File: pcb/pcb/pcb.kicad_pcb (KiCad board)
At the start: 2 copper layers, 58.4 x 44.4 mm, 20 parts, among them J1 UART, J2 Barrel_Jack, J3 Stepper, SW1 RESET, SW2 FLASH, U1 ESP32-WROOM-32, U2 TSR_1-2433

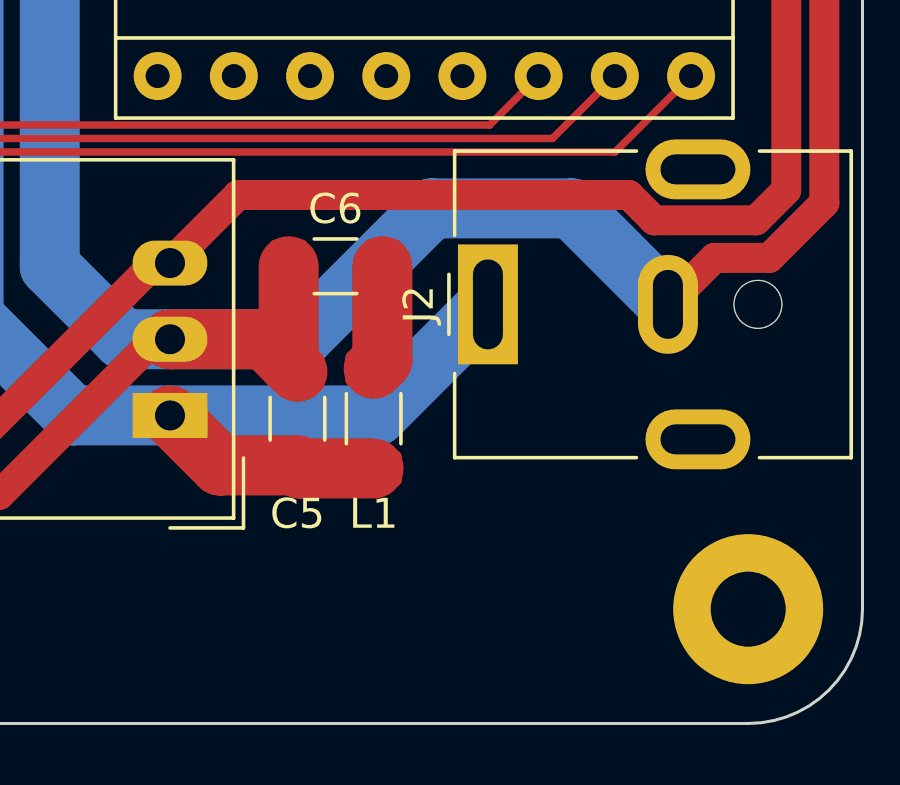
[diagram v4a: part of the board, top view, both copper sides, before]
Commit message: Add power led
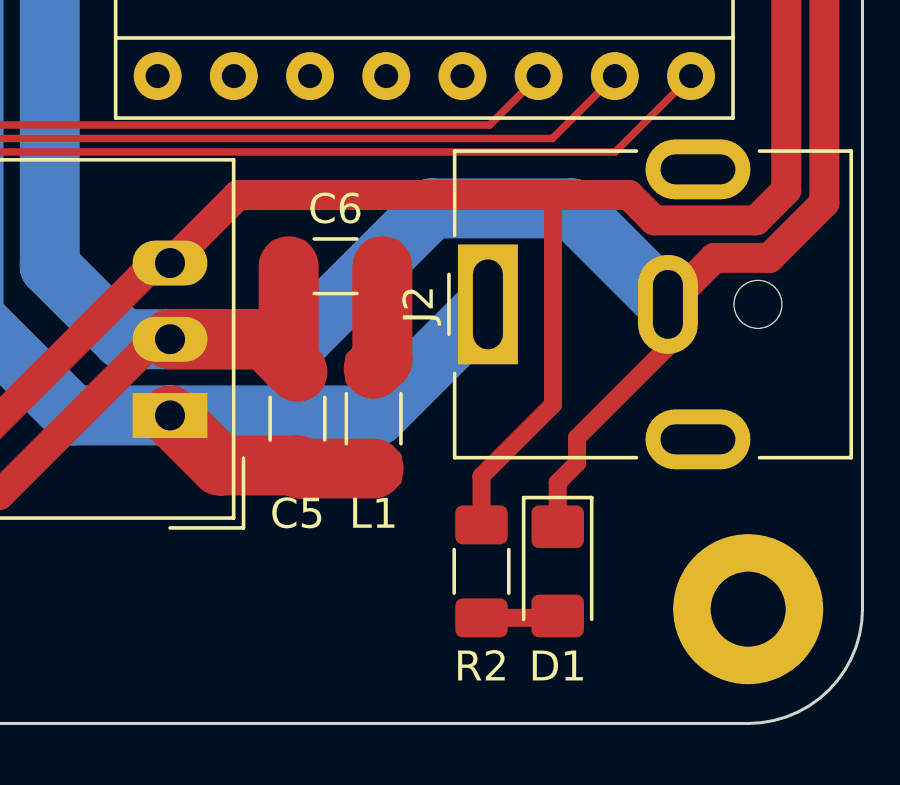
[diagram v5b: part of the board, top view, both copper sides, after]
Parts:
- added D1: LED, LED_SMD:LED_1206_3216Metric_Pad1.42x1.75mm_HandSolder, F.Cu at (125.7, 83.2)
- added R2: 650, Resistor_SMD:R_1206_3216Metric_Pad1.30x1.75mm_HandSolder, F.Cu at (123.2, 83.2)
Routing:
- net +3V3: track 84.3 -> 96.3 mm
- net GND: track 154.2 -> 163.2 mm
- net Net-(D1-Pad2): track 0.00 -> 2.57 mm
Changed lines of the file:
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@@
   (net 46 "unconnected-(U1-Pad36)")
   (net 47 "unconnected-(U1-Pad37)")
+  (net 48 "Net-(D1-Pad2)")
   (footprint "Module:Pololu_Breakout-16_15.2x20.3mm" (layer "F.Cu")
     (at 130.175 53.975 -90)
@@
       (net 15 "/DIR") (pinfunction "DIR") (pintype "input"))
     (model "${KICAD6_3DMODEL_DIR}/Module.3dshapes/Pololu_Breakout-16_15.2x20.3mm.wrl"
+      (offset (xyz 0 0 0))
+      (scale (xyz 1 1 1))
+      (rotate (xyz 0 0 0))
+    )
+  )
+  (footprint "LED_SMD:LED_1206_3216Metric_Pad1.42x1.75mm_HandSolder" (layer "F.Cu")
+    (at 125.73 83.185 -90)
+    (descr "LED SMD 1206 (3216 Metric), square (rectangular) end terminal, IPC_7351 nominal, (Body size source: http://www.tortai-tech.com/upload/download/2011102023233369053.pdf), generated with kicad-footprint-generator")
+    (tags "LED handsolder")
+    (property "Sheetfile" "pcb.kicad_sch")
+    (property "Sheetname" "")
+    (attr smd)
+    (fp_text reference "D1" (at 3.175 0 180) (layer "F.SilkS")
+      (effects (font (size 1 1) (thickness 0.15)))
+    )
+    (fp_text value "LED" (at 0 1.82 90) (layer "F.Fab")
+      (effects (font (size 1 1) (thickness 0.15)))
+    )
+    (fp_text user "${REFERENCE}" (at 0 0 90) (layer "F.Fab")
+      (effects (font (size 0.8 0.8) (thickness 0.12)))
+    )
+    (fp_line (start -2.46 -1.135) (end -2.46 1.135) (layer "F.SilkS") (width 0.12))
+    (fp_line (start -2.46 1.135) (end 1.6 1.135) (layer "F.SilkS") (width 0.12))
+    (fp_line (start 1.6 -1.135) (end -2.46 -1.135) (layer "F.SilkS") (width 0.12))
+    (fp_line (start -2.45 1.12) (end -2.45 -1.12) (layer "F.CrtYd") (width 0.05))
+    (fp_line (start -2.45 -1.12) (end 2.45 -1.12) (layer "F.CrtYd") (width 0.05))
+    (fp_line (start 2.45 1.12) (end -2.45 1.12) (layer "F.CrtYd") (width 0.05))
+    (fp_line (start 2.45 -1.12) (end 2.45 1.12) (layer "F.CrtYd") (width 0.05))
+    (fp_line (start -1.6 0.8) (end 1.6 0.8) (layer "F.Fab") (width 0.1))
+    (fp_line (start 1.6 -0.8) (end -1.2 -0.8) (layer "F.Fab") (width 0.1))
+    (fp_line (start 1.6 0.8) (end 1.6 -0.8) (layer "F.Fab") (width 0.1))
+    (fp_line (start -1.2 -0.8) (end -1.6 -0.4) (layer "F.Fab") (width 0.1))
+    (fp_line (start -1.6 -0.4) (end -1.6 0.8) (layer "F.Fab") (width 0.1))
+    (pad "1" smd roundrect (at -1.4875 0 270) (size 1.425 1.75) (layers "F.Cu" "F.Paste" "F.Mask") (roundrect_rratio 0.175439)
+      (net 2 "GND") (pinfunction "K") (pintype "passive"))
+    (pad "2" smd roundrect (at 1.4875 0 270) (size 1.425 1.75) (layers "F.Cu" "F.Paste" "F.Mask") (roundrect_rratio 0.175439)
+      (net 48 "Net-(D1-Pad2)") (pinfunction "A") (pintype "passive"))
+    (model "${KICAD6_3DMODEL_DIR}/LED_SMD.3dshapes/LED_1206_3216Metric.wrl"
+      (offset (xyz 0 0 0))
+      (scale (xyz 1 1 1))
+      (rotate (xyz 0 0 0))
+    )
+  )
+  (footprint "Resistor_SMD:R_1206_3216Metric_Pad1.30x1.75mm_HandSolder" (layer "F.Cu")
+    (at 123.19 83.185 -90)
+    (descr "Resistor SMD 1206 (3216 Metric), square (rectangular) end terminal, IPC_7351 nominal with elongated pad for handsoldering. (Body size source: IPC-SM-782 page 72, https://www.pcb-3d.com/wordpress/wp-content/uploads/ipc-sm-782a_amendment_1_and_2.pdf), generated with kicad-footprint-generator")
+    (tags "resistor handsolder")
+    (property "Sheetfile" "pcb.kicad_sch")
+    (property "Sheetname" "")
+    (attr smd)
+    (fp_text reference "R2" (at 3.175 0 180) (layer "F.SilkS")
+      (effects (font (size 1 1) (thickness 0.15)))
+    )
+    (fp_text value "650" (at 0 1.82 90) (layer "F.Fab")
+      (effects (font (size 1 1) (thickness 0.15)))
+    )
+    (fp_text user "${REFERENCE}" (at 0 0 90) (layer "F.Fab")
+      (effects (font (size 0.8 0.8) (thickness 0.12)))
+    )
+    (fp_line (start -0.727064 0.91) (end 0.727064 0.91) (layer "F.SilkS") (width 0.12))
+    (fp_line (start -0.727064 -0.91) (end 0.727064 -0.91) (layer "F.SilkS") (width 0.12))
+    (fp_line (start -2.45 1.12) (end -2.45 -1.12) (layer "F.CrtYd") (width 0.05))
+    (fp_line (start 2.45 1.12) (end -2.45 1.12) (layer "F.CrtYd") (width 0.05))
+    (fp_line (start -2.45 -1.12) (end 2.45 -1.12) (layer "F.CrtYd") (width 0.05))
+    (fp_line (start 2.45 -1.12) (end 2.45 1.12) (layer "F.CrtYd") (width 0.05))
+    (fp_line (start -1.6 -0.8) (end 1.6 -0.8) (layer "F.Fab") (width 0.1))
+    (fp_line (start -1.6 0.8) (end -1.6 -0.8) (layer "F.Fab") (width 0.1))
+    (fp_line (start 1.6 -0.8) (end 1.6 0.8) (layer "F.Fab") (width 0.1))
+    (fp_line (start 1.6 0.8) (end -1.6 0.8) (layer "F.Fab") (width 0.1))
+    (pad "1" smd roundrect (at -1.55 0 270) (size 1.3 1.75) (layers "F.Cu" "F.Paste" "F.Mask") (roundrect_rratio 0.192308)
+      (net 3 "+3V3") (pintype "passive"))
+    (pad "2" smd roundrect (at 1.55 0 270) (size 1.3 1.75) (layers "F.Cu" "F.Paste" "F.Mask") (roundrect_rratio 0.192308)
+      (net 48 "Net-(D1-Pad2)") (pintype "passive"))
+    (model "${KICAD6_3DMODEL_DIR}/Resistor_SMD.3dshapes/R_1206_3216Metric.wrl"
       (offset (xyz 0 0 0))
       (scale (xyz 1 1 1))
@@
   (segment (start 116.7625 76.24) (end 117.055 76.5325) (width 2) (layer "F.Cu") (net 2))
   (segment (start 93.6375 80.635) (end 90.53298 83.73952) (width 1) (layer "F.Cu") (net 2))
+  (segment (start 129.405 75.7) (end 129.405 74.285) (width 0.6) (layer "F.Cu") (net 2))
+  (segment (start 126.375278 79.580414) (end 126.375278 78.729722) (width 0.6) (layer "F.Cu") (net 2))
   (segment (start 94.17 46.79) (end 92.71 48.25) (width 0.25) (layer "F.Cu") (net 2))
+  (segment (start 126.375278 78.729722) (end 129.405 75.7) (width 0.6) (layer "F.Cu") (net 2))
   (segment (start 99.06 46.79) (end 104.775 46.79) (width 0.25) (layer "F.Cu") (net 2))
   (segment (start 107.12 80.635) (end 112.3075 75.4475) (width 1) (layer "F.Cu") (net 2))
@@
   (segment (start 134.62 60.32) (end 130.175 55.875) (width 1) (layer "F.Cu") (net 2))
   (segment (start 116.7625 73.015) (end 116.7625 76.24) (width 2) (layer "F.Cu") (net 2))
+  (segment (start 125.73 80.225692) (end 126.375278 79.580414) (width 0.6) (layer "F.Cu") (net 2))
   (segment (start 99.06 46.79) (end 94.17 46.79) (width 0.25) (layer "F.Cu") (net 2))
   (segment (start 129.405 74.285) (end 130.954521 72.735479) (width 1) (layer "F.Cu") (net 2))
   (segment (start 92.71 48.25) (end 86.575 48.25) (width 0.25) (layer "F.Cu") (net 2))
+  (segment (start 125.73 81.6975) (end 125.73 80.225692) (width 0.6) (layer "F.Cu") (net 2))
   (segment (start 132.785898 72.735479) (end 134.62 70.901377) (width 1) (layer "F.Cu") (net 2))
   (segment (start 85.895 48.93) (end 85.895 58.165) (width 0.25) (layer "F.Cu") (net 2))
@@
   (segment (start 97.37 78.73) (end 94.26 78.73) (width 1) (layer "F.Cu") (net 3))
   (segment (start 132.34048 71.48452) (end 133.35 70.475) (width 1) (layer "F.Cu") (net 3))
+  (segment (start 125.575758 70.639242) (end 128.105758 70.639242) (width 1) (layer "F.Cu") (net 3))
   (segment (start 133.35 70.475) (end 133.35 60.95) (width 1) (layer "F.Cu") (net 3))
   (segment (start 88.5575 78.095) (end 88.5575 80.635) (width 1) (layer "F.Cu") (net 3))
   (segment (start 87.165 76.7025) (end 88.5575 78.095) (width 1) (layer "F.Cu") (net 3))
+  (segment (start 123.19 80.01) (end 123.19 81.635) (width 0.6) (layer "F.Cu") (net 3))
+  (segment (start 115.075758 70.639242) (end 125.575758 70.639242) (width 1) (layer "F.Cu") (net 3))
+  (segment (start 125.575758 77.624242) (end 123.19 80.01) (width 0.6) (layer "F.Cu") (net 3))
   (segment (start 128.951036 71.48452) (end 132.34048 71.48452) (width 1) (layer "F.Cu") (net 3))
   (segment (start 98.005 79.365) (end 97.37 78.73) (width 1) (layer "F.Cu") (net 3))
@@
   (segment (start 94.26 78.73) (end 93.625 78.095) (width 1) (layer "F.Cu") (net 3))
   (segment (start 112.8075 72.9075) (end 115.075758 70.639242) (width 1) (layer "F.Cu") (net 3))
-  (segment (start 115.075758 70.639242) (end 128.105758 70.639242) (width 1) (layer "F.Cu") (net 3))
   (segment (start 127.635 55.235) (end 127.635 53.975) (width 1) (layer "F.Cu") (net 3))
   (segment (start 88.48 82.54) (end 88.48 80.7125) (width 1) (layer "F.Cu") (net 3))
   (segment (start 87.165 75.165) (end 87.165 76.7025) (width 1) (layer "F.Cu") (net 3))
+  (segment (start 125.575758 70.639242) (end 125.575758 77.624242) (width 0.6) (layer "F.Cu") (net 3))
   (segment (start 112.3075 72.9075) (end 106.485 78.73) (width 1) (layer "F.Cu") (net 3))
   (segment (start 88.48 80.7125) (end 88.5575 80.635) (width 1) (layer "F.Cu") (net 3))
@@
   (segment (start 99.06 53.19) (end 102.405 56.535) (width 0.25) (layer "F.Cu") (net 36))
   (segment (start 102.405 56.535) (end 102.405 58.165) (width 0.25) (layer "F.Cu") (net 36))
+  (segment (start 125.6675 84.735) (end 125.73 84.6725) (width 0.6) (layer "F.Cu") (net 48))
+  (segment (start 123.19 84.735) (end 125.6675 84.735) (width 0.6) (layer "F.Cu") (net 48))
 )

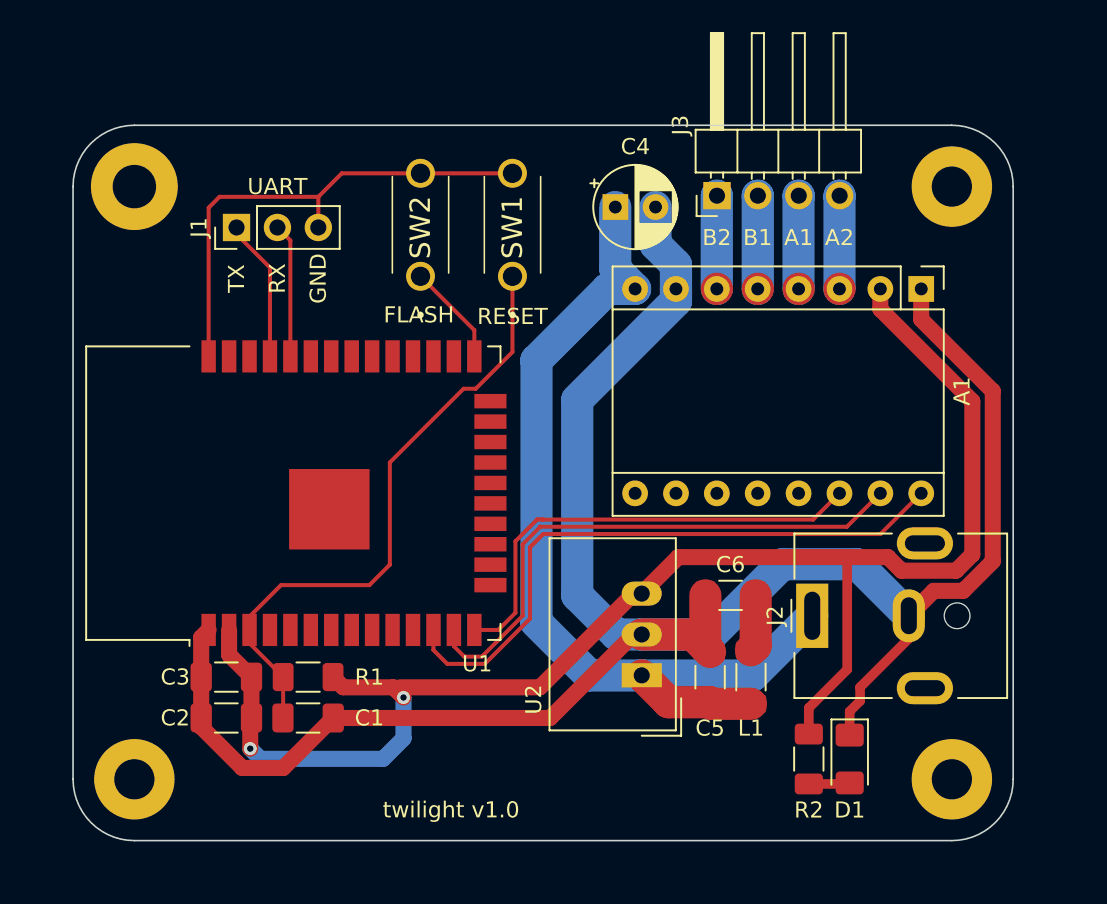
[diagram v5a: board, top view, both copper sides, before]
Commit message: add copper pours
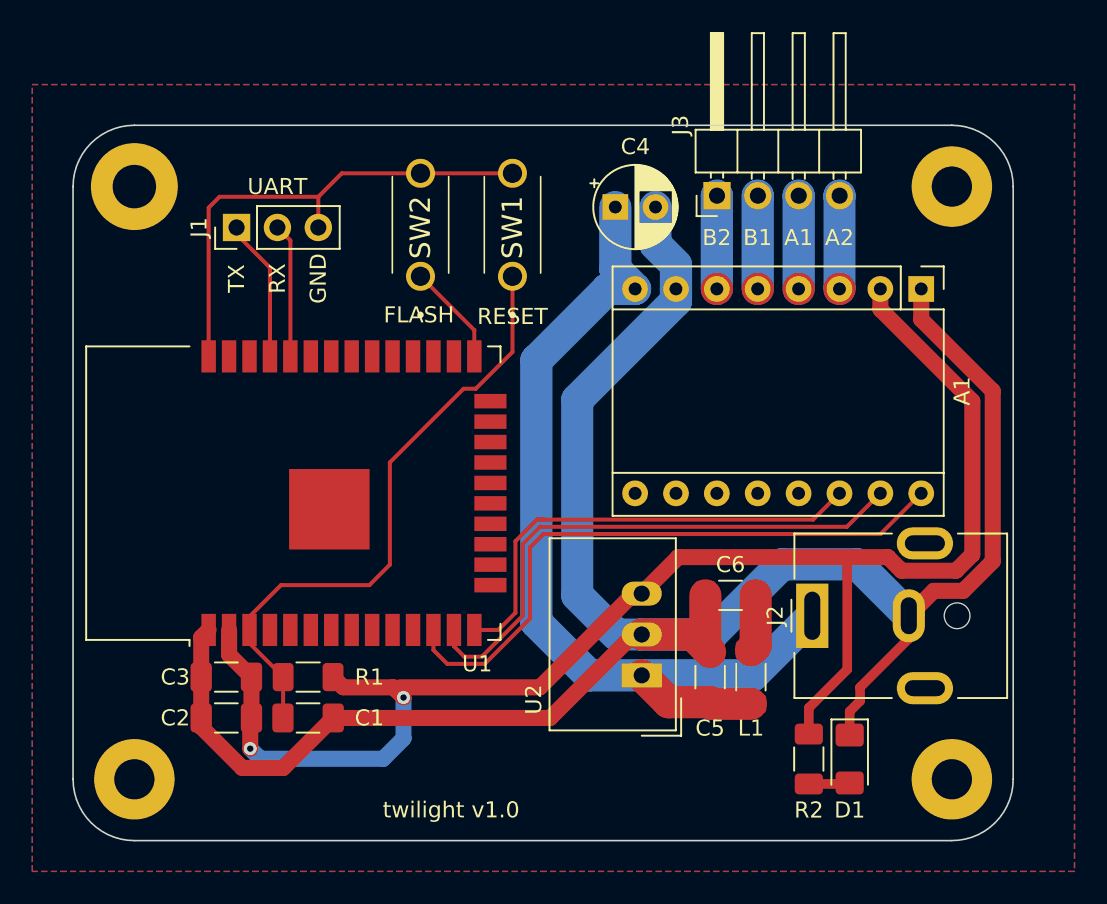
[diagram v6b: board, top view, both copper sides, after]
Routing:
- added copper zone on B.Cu, net GND
- added copper zone on F.Cu, net GND
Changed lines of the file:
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@@
   (segment (start 125.6675 84.735) (end 125.73 84.6725) (width 0.6) (layer "F.Cu") (net 48))
   (segment (start 123.19 84.735) (end 125.6675 84.735) (width 0.6) (layer "F.Cu") (net 48))
+  (zone (net 2) (net_name "GND") (layers F&B.Cu) (hatch edge 0.508)
+    (connect_pads (clearance 0.508))
+    (min_thickness 0.254) (filled_areas_thickness no)
+    (fill yes (thermal_gap 0.508) (thermal_bridge_width 0.508))
+    (polygon
+      (pts
+        (xy 139.7 90.17)
+        (xy 74.93 90.17)
+        (xy 74.93 41.275)
+        (xy 139.7 41.275)
+      )
+    )
+  )
 )

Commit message: tweaks from reddit wiki
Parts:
- H1: footprint MountingHole:MountingHole_2.7mm_M2.5_Pad -> MountingHole:MountingHole_3.2mm_M3_DIN965_Pad
- H2, H3, H4: footprint MountingHole:MountingHole_2.5mm_Pad -> MountingHole:MountingHole_3.2mm_M3_DIN965_Pad
- moved C1 3.81 mm to (95.9, 80.6)
- moved R1 3.81 mm to (95.9, 78.1)
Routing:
- net /EN: track 38.7 -> 42.6 mm
- net GND: track 163.2 -> 166.9 mm
- removed copper zone on B.Cu, net GND
- removed copper zone on F.Cu, net GND
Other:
- board text added: "PWR"

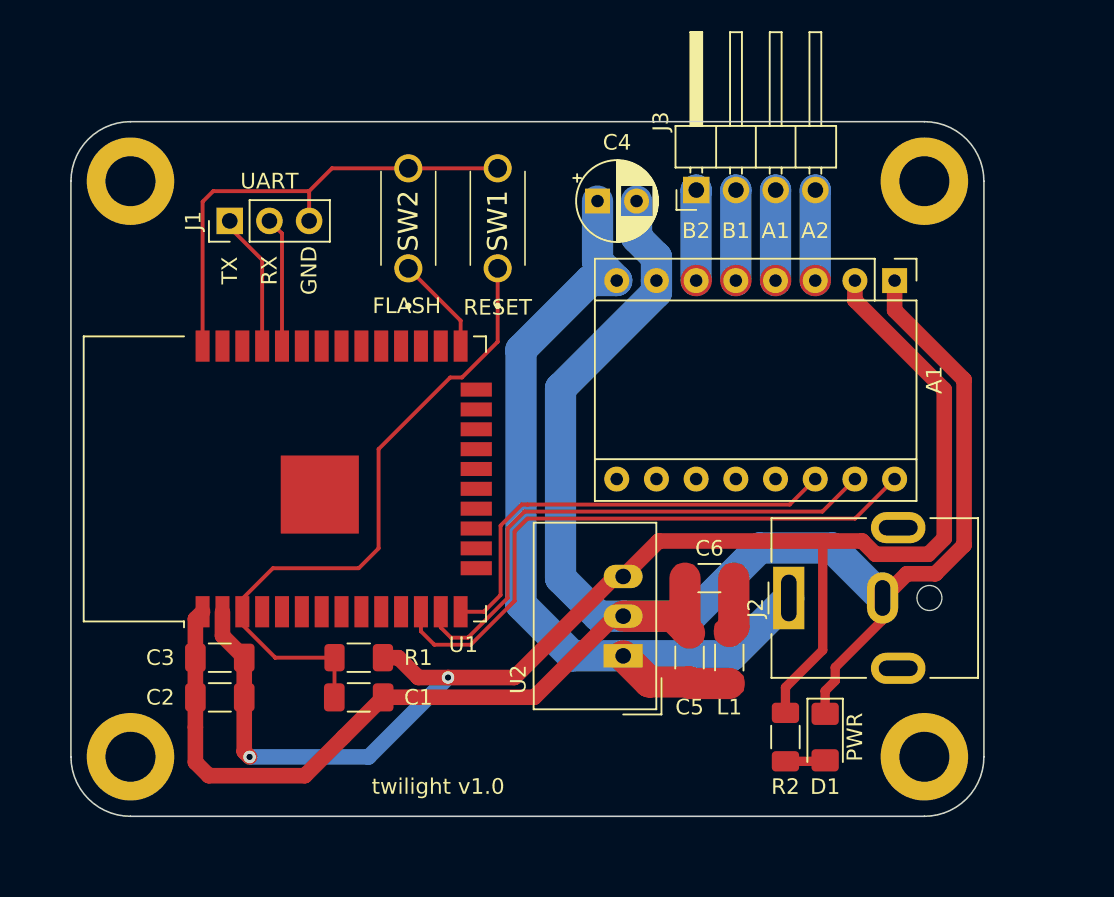
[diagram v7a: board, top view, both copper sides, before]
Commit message: add activity led and general tidy
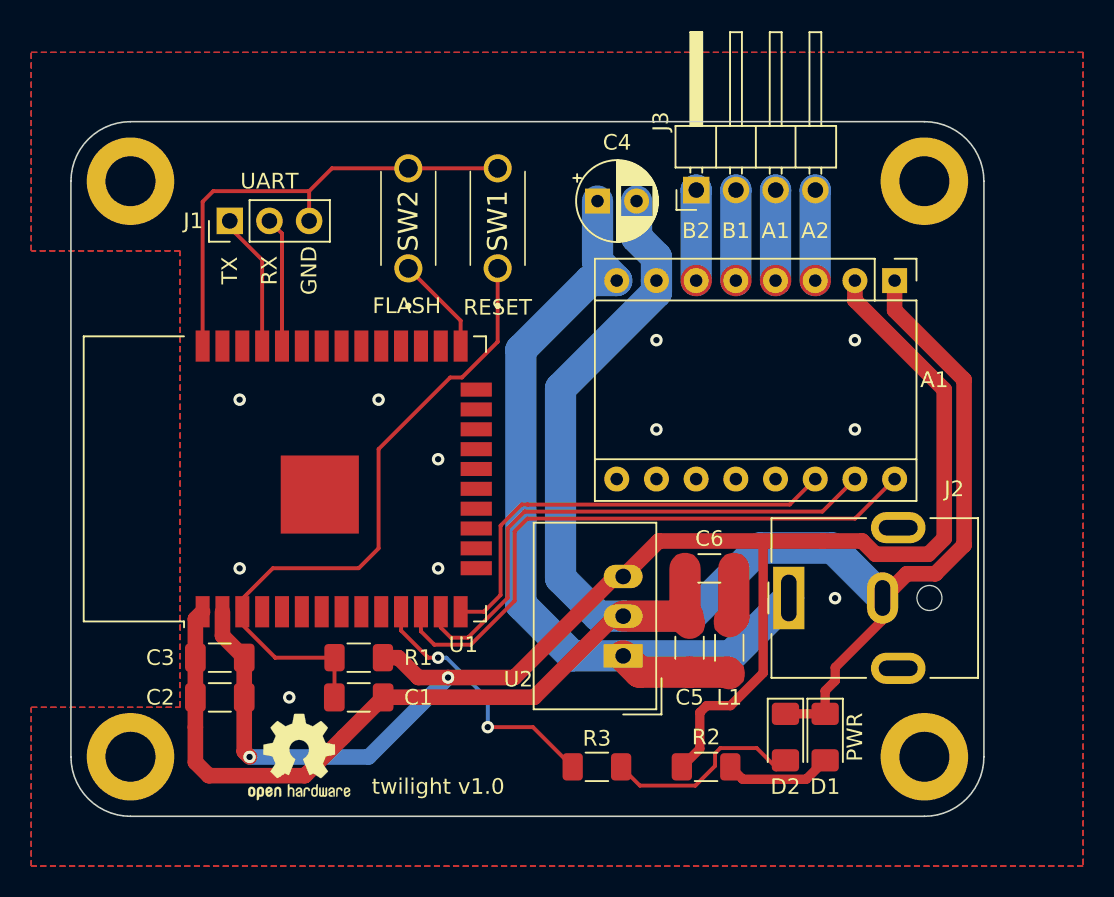
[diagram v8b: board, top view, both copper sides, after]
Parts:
- added D2: LED GREEN, LED_SMD:LED_1206_3216Metric_Pad1.42x1.75mm_HandSolder, F.Cu at (123.2, 83.2)
- added R3: 650, Resistor_SMD:R_1206_3216Metric_Pad1.30x1.75mm_HandSolder, F.Cu at (111.1, 85.1)
- added REF**: OSHW-Logo2_7.3x6mm_SilkScreen, Symbol:OSHW-Logo2_7.3x6mm_SilkScreen, F.Cu at (92.1, 84.5)
- D1: value LED -> LED RED
- moved R2 5.43 mm to (118.1, 85.1), turned to 0 degrees
- moved C5 0.62 mm to (117.1, 77.5)
- moved C6 0.62 mm to (118.3, 72.4)
- moved L1 0.62 mm to (119.6, 77.5)
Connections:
- U1 pad 11: unconnected-(U1-Pad11) -> Net-(U1-Pad11)
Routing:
- net Net-(U1-Pad11): track 0.00 -> 16.9 mm, vias 0 -> 2
- net Net-(D2-Pad2): track 0.00 -> 12.5 mm
- net +3V3: track 96.5 -> 102.0 mm
- net Net-(D1-Pad2): track 2.57 -> 6.90 mm
- net GND: track 166.9 -> 169.3 mm, vias 0 -> 11
- added copper zone on B.Cu, net GND
- added copper zone on F.Cu, net GND
